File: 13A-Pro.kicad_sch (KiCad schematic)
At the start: 16 parts, among them SW1 SW_Push, U1 ProMicro

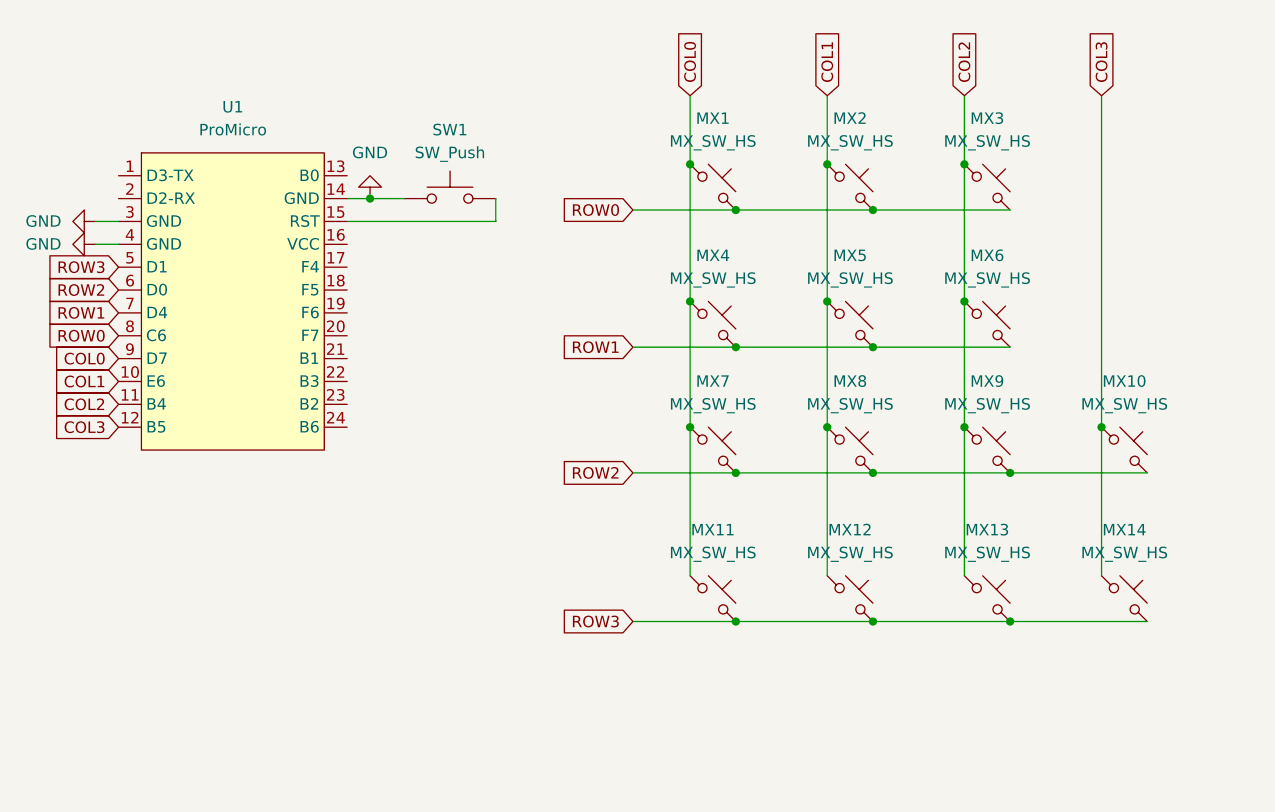
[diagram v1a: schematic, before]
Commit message: Footprints assigning
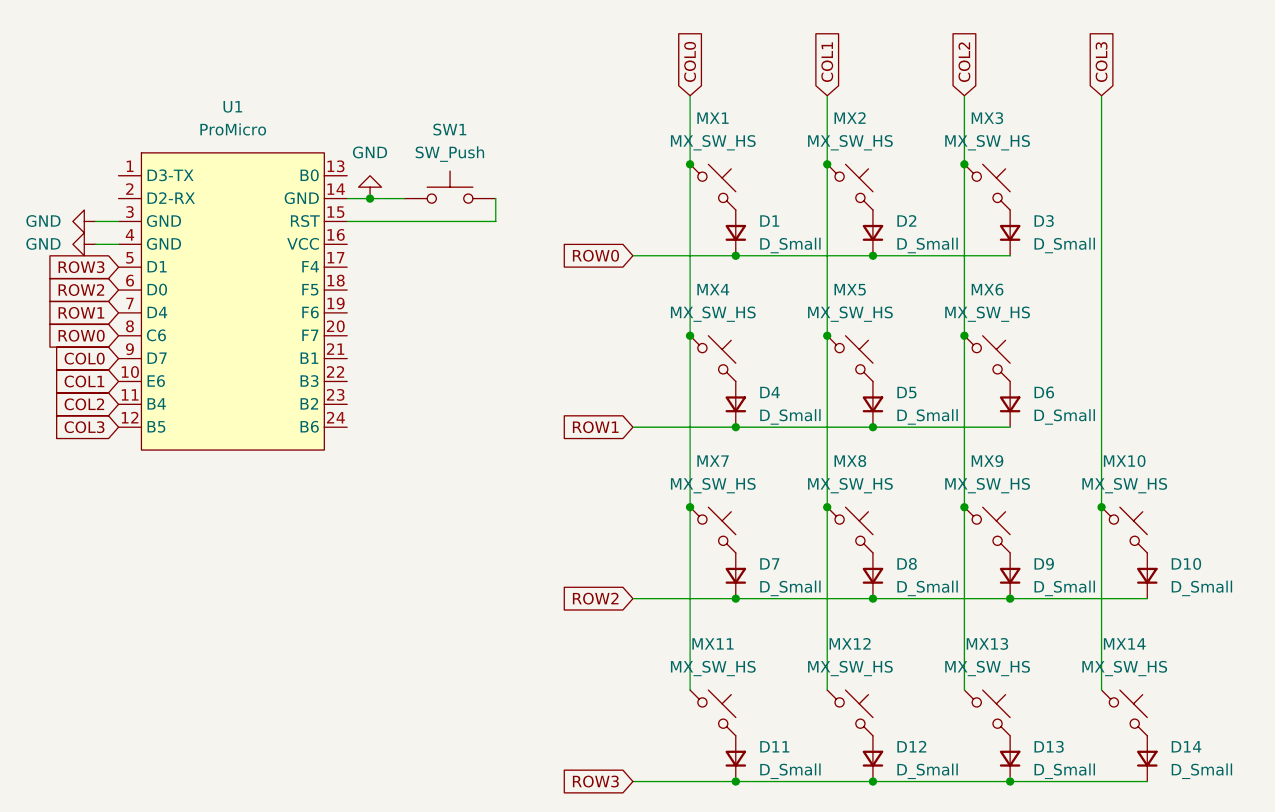
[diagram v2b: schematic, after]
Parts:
- added D1, D10, D11, D12, D13, D14, D2, D3, D4, D5, D6, D7, D8, D9: D_Small, Diode_SMD:D_SOD-123, symbol Device:D_Small
- MX1, MX10, MX11, MX12, MX13, MX14, MX2, MX3, MX4, MX5, MX6, MX7, MX8, MX9: footprint PCM_marbastlib-mx:SW_MX_HS_1u -> marbastlib-mx:SW_MX_HS_1u
- SW1: footprint (none) -> Button_Switch_SMD:SW_SPST_PTS810
- U1: footprint PCM_marbastlib-xp-promicroish:ProMicro_USBup -> marbastlib-xp-promicroish:ProMicro_USBup
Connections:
- net ROW0: now also D1.1 (K), D2.1 (K), D3.1 (K); no longer MX1.2, MX2.2, MX3.2
- net ROW1: now also D4.1 (K), D5.1 (K), D6.1 (K); no longer MX4.2, MX5.2, MX6.2
- net ROW2: now also D10.1 (K), D7.1 (K), D8.1 (K), D9.1 (K); no longer MX10.2, MX7.2, MX8.2, MX9.2
- net ROW3: now also D11.1 (K), D12.1 (K), D13.1 (K), D14.1 (K); no longer MX11.2, MX12.2, MX13.2, MX14.2
- new net: D2.2 (A), MX2.2
- new net: D11.2 (A), MX11.2
- new net: D13.2 (A), MX13.2
- new net: D10.2 (A), MX10.2
- new net: D5.2 (A), MX5.2
- new net: D12.2 (A), MX12.2
- new net: D14.2 (A), MX14.2
- new net: D7.2 (A), MX7.2
- new net: D8.2 (A), MX8.2
- new net: D9.2 (A), MX9.2
- new net: D6.2 (A), MX6.2
- new net: D3.2 (A), MX3.2
- new net: D4.2 (A), MX4.2
- new net: D1.2 (A), MX1.2
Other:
- moved on the sheet: MX10, MX11, MX12, MX13, MX14, MX4, MX5, MX6, MX7, MX8, MX9

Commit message: PCB Update
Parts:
- SW1: footprint Button_Switch_SMD:SW_SPST_PTS810 -> Switches:TACTILE_SWITCH_SMD_6.0X3.5MM
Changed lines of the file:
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@@
       (effects (font (size 1.27 1.27)))
     )
-    (property "Footprint" "Button_Switch_SMD:SW_SPST_PTS810" (at 90.17 49.53 0)
+    (property "Footprint" "Switches:TACTILE_SWITCH_SMD_6.0X3.5MM" (at 90.17 49.53 0)
       (effects (font (size 1.27 1.27)) hide)
     )

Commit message: PCB Update ver 1.0
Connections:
- net ROW0: now also U1.5 (D1); no longer U1.8 (C6)
- net ROW1: now also U1.6 (D0); no longer U1.7 (D4)
- net ROW2: now also U1.7 (D4); no longer U1.6 (D0)
- net ROW3: now also U1.8 (C6); no longer U1.5 (D1)
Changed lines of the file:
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@@
     (stroke (width 0) (type default))
   )
-  (global_label "ROW2" (shape input) (at 53.34 64.77 180) (fields_autoplaced)
+  (global_label "ROW2" (shape input) (at 53.34 67.31 180) (fields_autoplaced)
     (effects (font (size 1.27 1.27)) (justify right))
-    (property "Intersheetrefs" "${INTERSHEET_REFS}" (at 45.1728 64.77 0)
+    (property "Intersheetrefs" "${INTERSHEET_REFS}" (at 45.1728 67.31 0)
       (effects (font (size 1.27 1.27)) (justify right) hide)
     )
@@
     )
   )
-  (global_label "ROW0" (shape input) (at 53.34 69.85 180) (fields_autoplaced)
+  (global_label "ROW0" (shape input) (at 53.34 62.23 180) (fields_autoplaced)
     (effects (font (size 1.27 1.27)) (justify right))
-    (property "Intersheetrefs" "${INTERSHEET_REFS}" (at 45.1728 69.85 0)
+    (property "Intersheetrefs" "${INTERSHEET_REFS}" (at 45.1728 62.23 0)
       (effects (font (size 1.27 1.27)) (justify right) hide)
     )
@@
     )
   )
-  (global_label "ROW3" (shape input) (at 53.34 62.23 180) (fields_autoplaced)
+  (global_label "ROW3" (shape input) (at 53.34 69.85 180) (fields_autoplaced)
     (effects (font (size 1.27 1.27)) (justify right))
-    (property "Intersheetrefs" "${INTERSHEET_REFS}" (at 45.1728 62.23 0)
+    (property "Intersheetrefs" "${INTERSHEET_REFS}" (at 45.1728 69.85 0)
       (effects (font (size 1.27 1.27)) (justify right) hide)
     )
   )
-  (global_label "ROW1" (shape input) (at 53.34 67.31 180) (fields_autoplaced)
+  (global_label "ROW1" (shape input) (at 53.34 64.77 180) (fields_autoplaced)
     (effects (font (size 1.27 1.27)) (justify right))
-    (property "Intersheetrefs" "${INTERSHEET_REFS}" (at 45.1728 67.31 0)
+    (property "Intersheetrefs" "${INTERSHEET_REFS}" (at 45.1728 64.77 0)
       (effects (font (size 1.27 1.27)) (justify right) hide)
     )

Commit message: Case, PCB, Firmware update
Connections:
- net COL1: now also U1.11 (B4); no longer U1.10 (E6)
- net COL2: now also U1.10 (E6); no longer U1.11 (B4)
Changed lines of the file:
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@@
     )
   )
-  (global_label "COL1" (shape input) (at 53.34 74.93 180) (fields_autoplaced)
+  (global_label "COL1" (shape input) (at 53.34 77.47 180) (fields_autoplaced)
     (effects (font (size 1.27 1.27)) (justify right))
-    (property "Intersheetrefs" "${INTERSHEET_REFS}" (at 45.5961 74.93 0)
+    (property "Intersheetrefs" "${INTERSHEET_REFS}" (at 45.5961 77.47 0)
       (effects (font (size 1.27 1.27)) (justify right) hide)
     )
@@
     )
   )
-  (global_label "COL2" (shape input) (at 53.34 77.47 180) (fields_autoplaced)
+  (global_label "COL2" (shape input) (at 53.34 74.93 180) (fields_autoplaced)
     (effects (font (size 1.27 1.27)) (justify right))
-    (property "Intersheetrefs" "${INTERSHEET_REFS}" (at 45.5961 77.47 0)
+    (property "Intersheetrefs" "${INTERSHEET_REFS}" (at 45.5961 74.93 0)
       (effects (font (size 1.27 1.27)) (justify right) hide)
     )
